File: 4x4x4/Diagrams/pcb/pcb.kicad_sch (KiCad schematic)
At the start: 81 parts

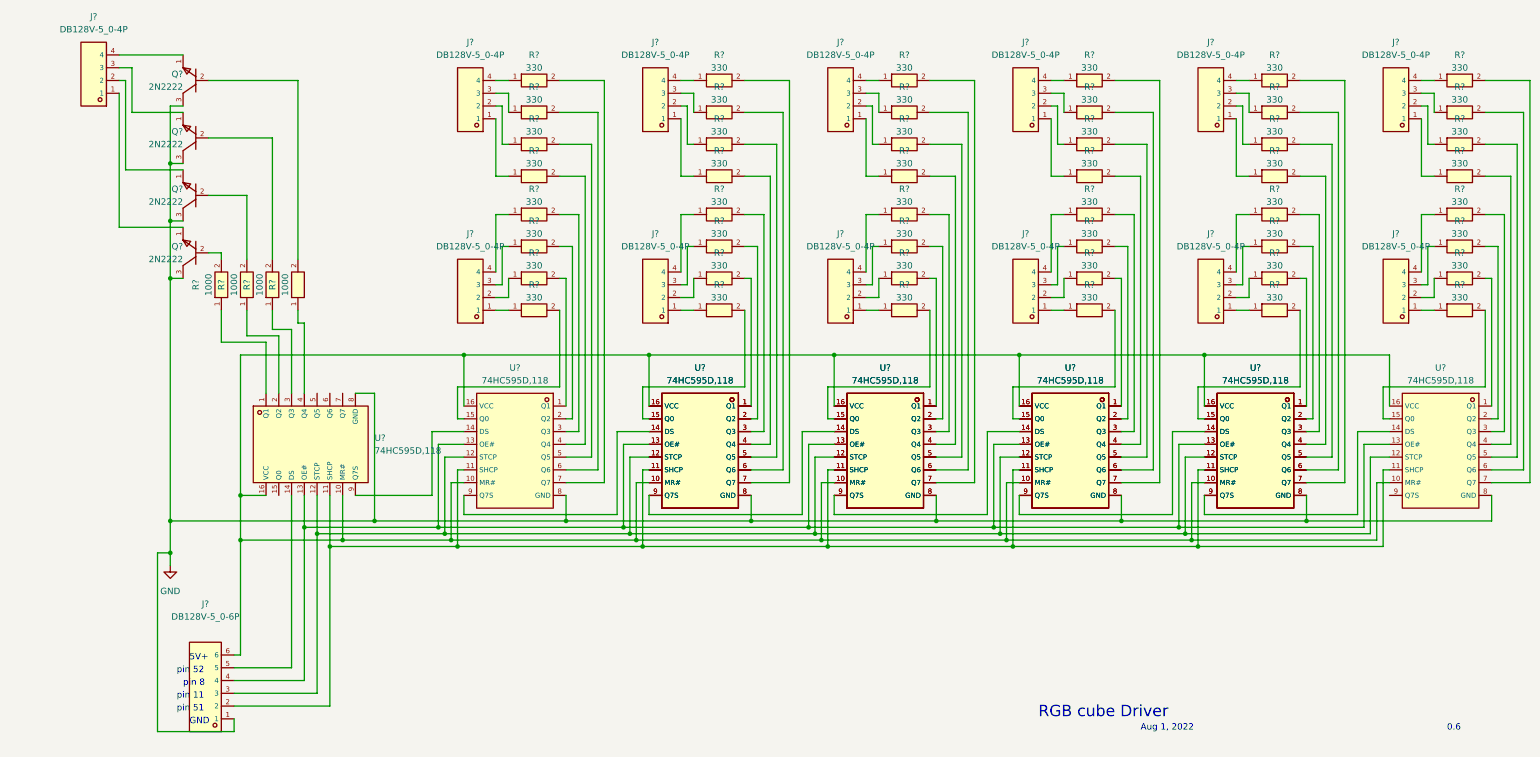
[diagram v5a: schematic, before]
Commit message: redesign schematic
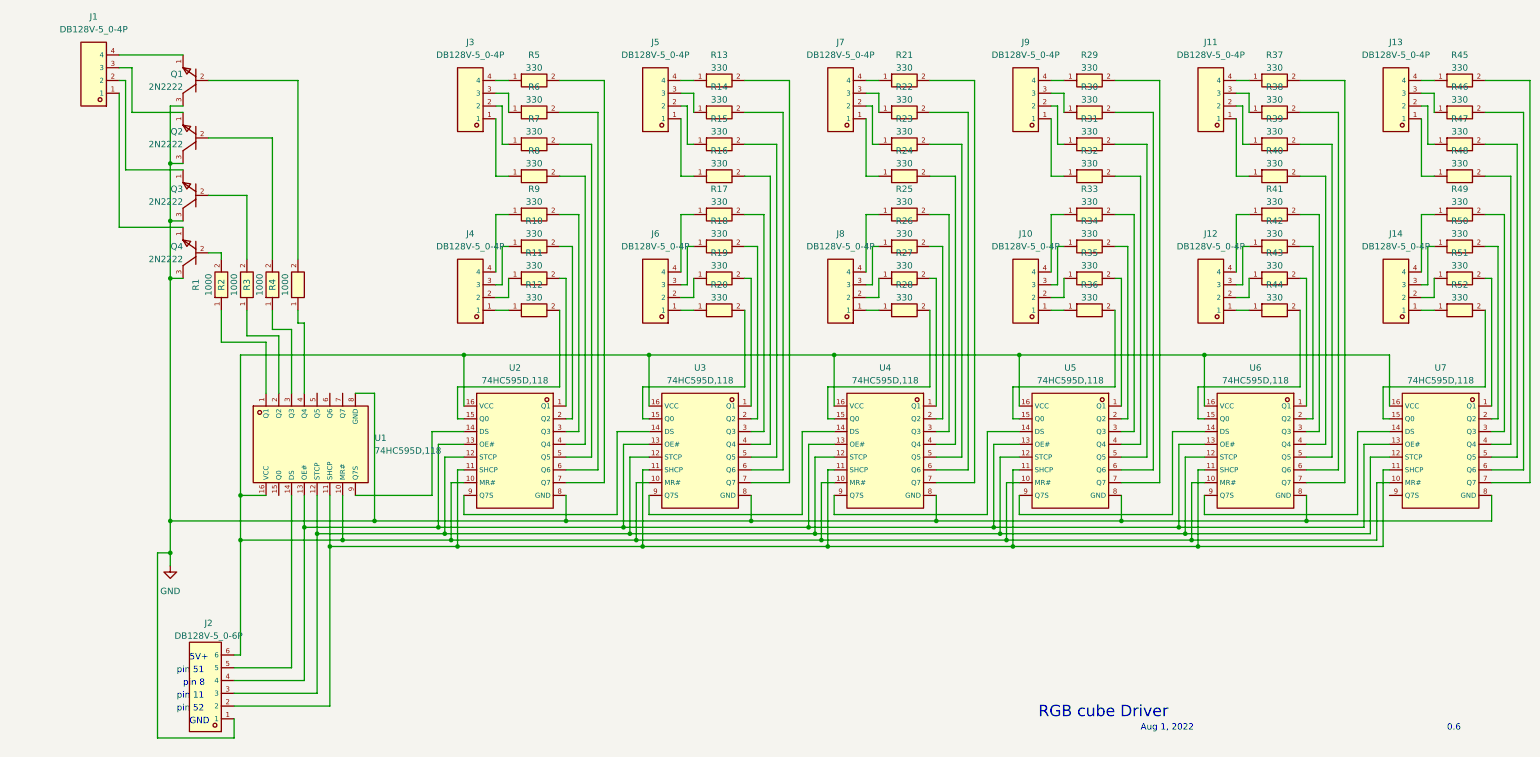
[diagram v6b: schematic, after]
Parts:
- removed U? (x9): 74HC595D,118, footprint:SOIC-16_L9.9-W3.9-P1.27-LS6.0-BL, symbol 74HC595D,118:74HC595D,118
- added U3, U4, U5, U6, U7: 74HC595D,118, 74HC595:SOIC-16_L9.9-W3.9-P1.27-LS6.0-BL, symbol 74HC595D,118:74HC595D,118
- J1, J10, J11, J12, J13, J14, J3, J4, J5, J6, J7, J8, J9: renamed from J?; footprint footprint:CONN-TH_DB128V-5.0-4P -> DB128V-5.0-4P-GN-S:CONN-TH_DB128V-5.0-4P
- J2: renamed from J?; footprint footprint:CONN-TH_6P-P5.00_DB128V -> DB128V-5.0-6P-GN-S:CONN-TH_6P-P5.00_DB128V
- Q1, Q2, Q3, Q4: renamed from Q?; footprint footprint:TO-92-3_L4.9-W3.7-P1.27-L -> 2N2222A:TO-92-3_L4.9-W3.7-P1.27-L
- R1, R2, R3, R4: renamed from R?; footprint footprint:RES-TH_BD2.4-L6.3-P10.30-D0.6 -> 1kR:RES-TH_BD2.4-L6.3-P10.30-D0.6
- R10, R11, R12, R13, R14, R15, R16, R17, R18, R19, R20, R21, R22, R23, R24, R25, R26, R27, R28, R29, R30, R31, R32, R33, R34, R35, R36, R37, R38, R39, R40, R41, R42, R43, R44, R45, R46, R47, R48, R49, R5, R50, R51, R52, R6, R7, R8, R9: renamed from R?; footprint footprint:RES-TH_BD2.4-L6.3-P10.30-D0.6 -> 330R:RES-TH_BD2.4-L6.3-P10.30-D0.6
- U1, U2: renamed from U?; footprint footprint:SOIC-16_L9.9-W3.9-P1.27-LS6.0-BL -> 74HC595:SOIC-16_L9.9-W3.9-P1.27-LS6.0-BL
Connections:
- net GND: now also U3.8 (GND), U4.8 (GND), U5.8 (GND), U6.8 (GND), U7.8 (GND)
- net at R39.2: now also U6.5 (Q5)
- net at R43.2: now also U6.1 (Q1)
- net at R50.2: now also U7.2 (Q2)
- net at R51.2: now also U7.1 (Q1)
- net at R35.2: now also U5.1 (Q1)
- net at R13.2: now also U3.7 (Q7)
- net at J2.6, U1.10 (MR#), U1.16 (VCC)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: now also U3.10 (MR#), U3.16 (VCC), U4.10 (MR#), U4.16 (VCC), U5.10 (MR#), U5.16 (VCC), U6.10 (MR#), U6.16 (VCC), U7.10 (MR#), U7.16 (VCC)
- net at J2.2, U1.11 (SHCP), U2.11 (SHCP): now also U3.11 (SHCP), U4.11 (SHCP), U5.11 (SHCP), U6.11 (SHCP), U7.11 (SHCP)
- net at J2.3, U1.12 (STCP), U2.12 (STCP): now also U3.12 (STCP), U4.12 (STCP), U5.12 (STCP), U6.12 (STCP), U7.12 (STCP)
- net at J2.4, U1.13 (OE#), U2.13 (OE#): now also U3.13 (OE#), U4.13 (OE#), U5.13 (OE#), U6.13 (OE#), U7.13 (OE#)
- net at R44.2: now also U6.15 (Q0)
- net at R42.2: now also U6.2 (Q2)
- net at R41.2: now also U6.3 (Q3)
- net at R40.2: now also U6.4 (Q4)
- net at R38.2: now also U6.6 (Q6)
- net at R37.2: now also U6.7 (Q7)
- net at R36.2: now also U5.15 (Q0)
- net at R34.2: now also U5.2 (Q2)
- net at R33.2: now also U5.3 (Q3)
- net at R32.2: now also U5.4 (Q4)
- net at R31.2: now also U5.5 (Q5)
- net at R30.2: now also U5.6 (Q6)
- net at R29.2: now also U5.7 (Q7)
- net at R23.2: now also U4.5 (Q5)
- net at R24.2: now also U4.4 (Q4)
- net at R25.2: now also U4.3 (Q3)
- net at R19.2: now also U3.1 (Q1)
- net at U2.9 (Q7S): now also U3.14 (DS)
- net at R20.2: now also U3.15 (Q0)
- net at R18.2: now also U3.2 (Q2)
- net at R17.2: now also U3.3 (Q3)
- net at R16.2: now also U3.4 (Q4)
- net at R15.2: now also U3.5 (Q5)
- net at R14.2: now also U3.6 (Q6)
- net at R27.2: now also U4.1 (Q1)
- net at R21.2: now also U4.7 (Q7)
- net at R22.2: now also U4.6 (Q6)
- net at R28.2: now also U4.15 (Q0)
- net at R52.2: now also U7.15 (Q0)
- net at R49.2: now also U7.3 (Q3)
- net at R48.2: now also U7.4 (Q4)
- net at R47.2: now also U7.5 (Q5)
- net at R46.2: now also U7.6 (Q6)
- net at R45.2: now also U7.7 (Q7)
- net at R26.2: now also U4.2 (Q2)
- new net: U3.9 (Q7S), U4.14 (DS)
- new net: U4.9 (Q7S), U5.14 (DS)
- new net: U5.9 (Q7S), U6.14 (DS)
- new net: U6.9 (Q7S), U7.14 (DS)
